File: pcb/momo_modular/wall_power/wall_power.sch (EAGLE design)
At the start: 18 parts

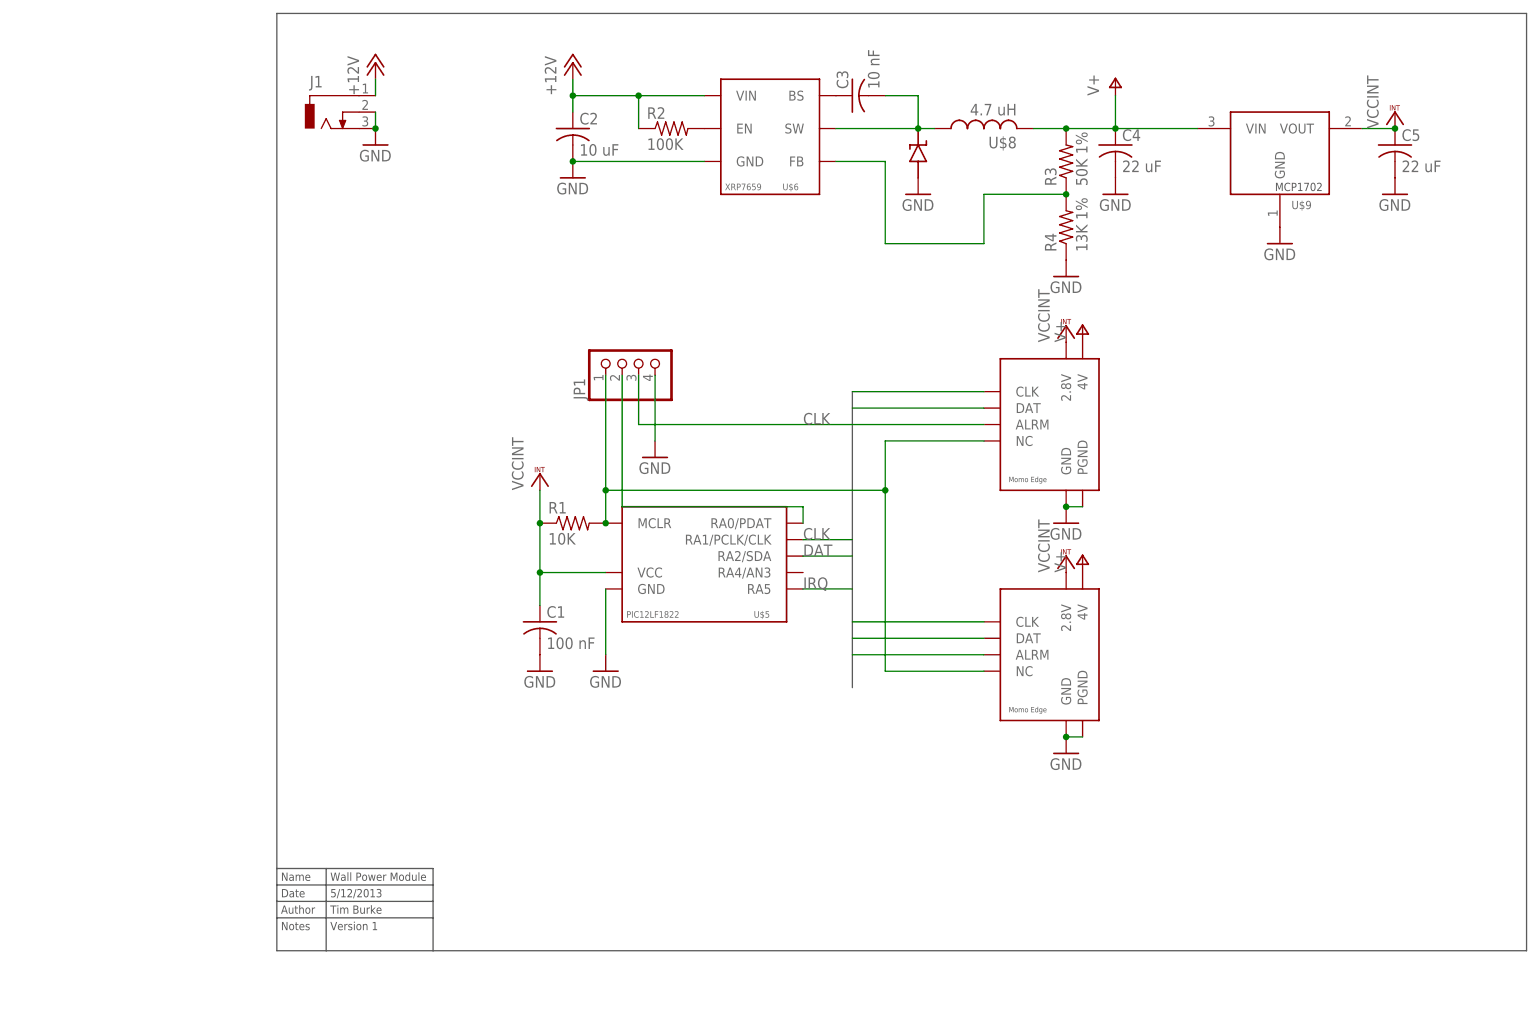
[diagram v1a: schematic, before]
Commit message: Began combining wallpower and controller boards
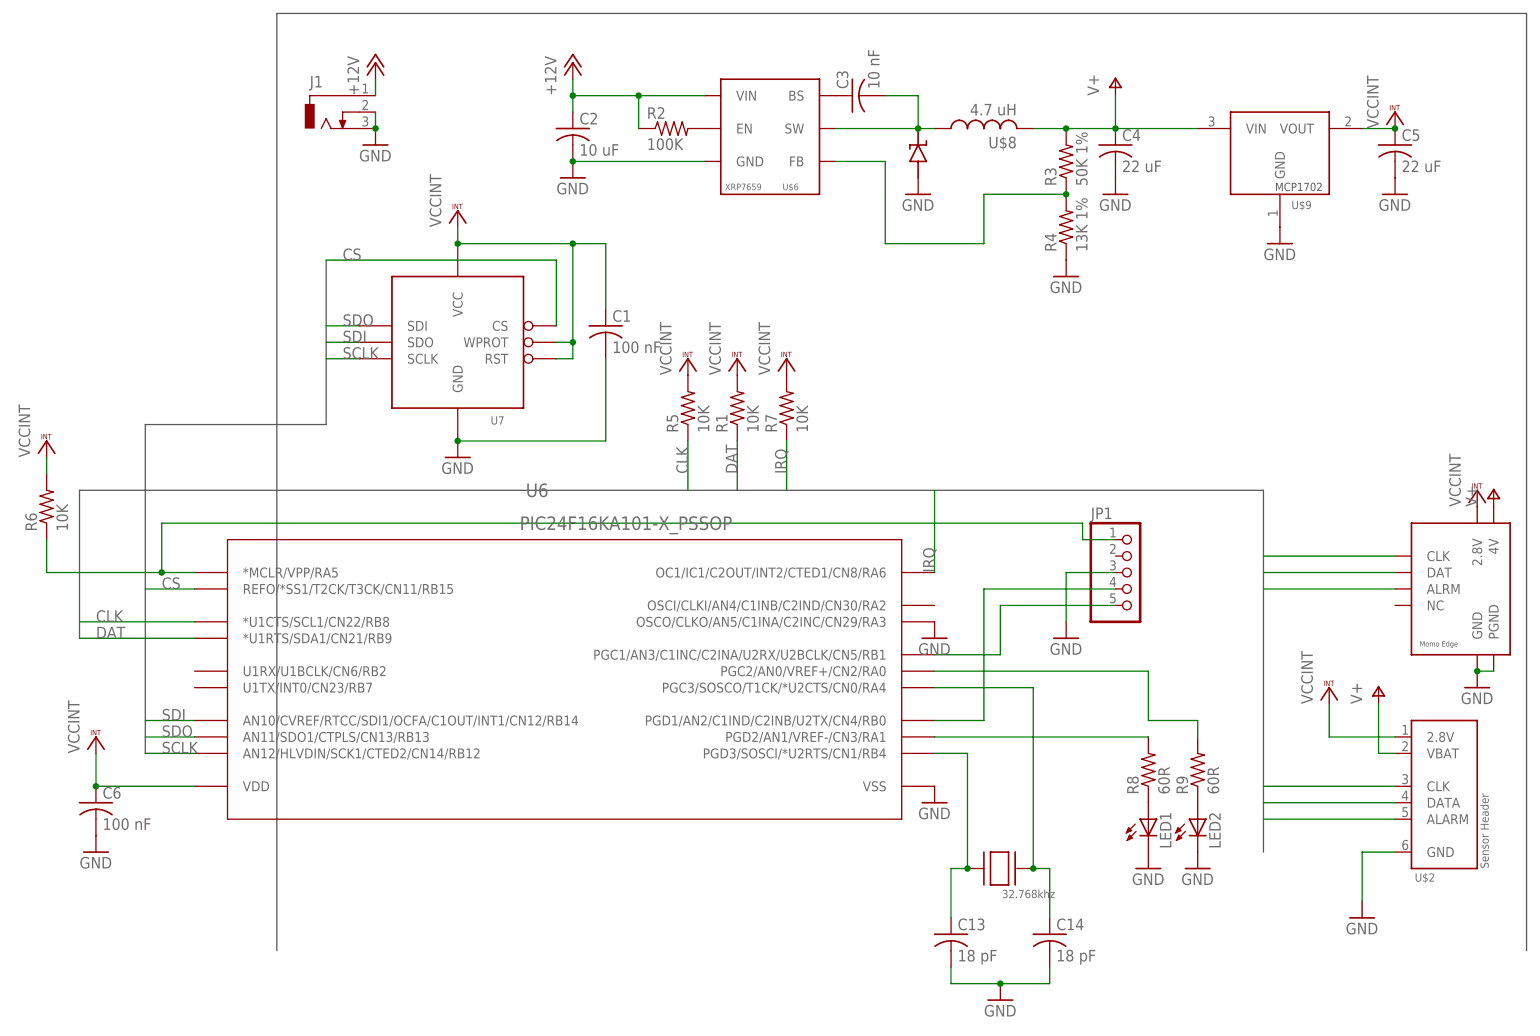
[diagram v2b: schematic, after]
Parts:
- removed U$5: PIC12LF1822, components:PIC12LF1822
- added C13, C14: 18 pF, rcl:C-USC0402K
- added C6: 100 nF, rcl:C-USC0402
- added LED1, LED2: (no value), led:LEDSML0603
- added R5, R6, R7: 10K, rcl:R-US_R0603
- added R8, R9: 60R, rcl:R-US_R0603
- added U6: PIC24F16KA101-X_PSSOP, components:PIC24F16KA101-X_PSSOP
- added U7: FLASH8MSOP8, components:FLASH8MSOP8
- added XTAL1: 32.768khz, components:SMD-XTAL
- JP1: device pinhead:PINHD-1X4 -> pinhead:PINHD-1X5
- U$2: value MOMO-EDGE-8M -> MOMO-SENSOR-HEADER; device components:MOMO-EDGE-8M -> components:MOMO-SENSOR-HEADER
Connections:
- new net CS: U6.REFO/*SS1/T2CK/T3CK/CN11/RB15, U7.CS
- new net N$10: JP1.5, U6.PGC1/AN3/C1INC/C2INA/U2RX/U2BCLK/CN5/RB1
- new net N$15: JP1.1, R6.1, U6.*MCLR/VPP/RA5
- new net N$24: C14.1, U6.PGC3/SOSCO/T1CK/*U2CTS/CN0/RA4, XTAL1.XTAL2
- new net N$25: C13.1, U6.PGD3/SOSCI/*U2RTS/CN1/RB4, XTAL1.XTAL1
- new net N$5: LED2.A, R9.1
- new net N$7: LED1.A, R8.1
- new net N$9: JP1.4, U6.PGD1/AN2/C1IND/C2INB/U2TX/CN4/RB0
- new net SCLK: U6.AN12/HLVDIN/SCK1/CTED2/CN14/RB12, U7.SCLK
- new net SDI: U6.AN10/CVREF/RTCC/SDI1/OCFA/C1OUT/INT1/CN12/RB14, U7.SDO
- new net SDO: U6.AN11/SDO1/CTPLS/CN13/RB13, U7.SDI
- net CLK: now also R5.1, U6.*U1CTS/SCL1/CN22/RB8; no longer JP1.3, U$5.RA1/PCLK/CLK
- net DAT: now also R1.1, U$2.DATA, U6.*U1RTS/SDA1/CN21/RB9; no longer U$2.DAT, U$5.RA2/SDA
- net GND: now also C13.2, C14.2, C6.2, JP1.3, LED1.C, LED2.C, U6.OSCO/CLKO/AN5/C1INA/C2INC/CN29/RA3, U6.VSS, U7.GND; no longer JP1.4, U$2.PGND, U$5.GND
- net IRQ: now also R7.1, U$2.ALARM, U6.OC1/IC1/C2OUT/INT2/CTED1/CN8/RA6; no longer U$2.ALRM, U$5.RA5
- net N$1: now also R9.2, U6.PGC2/AN0/VREF+/CN2/RA0; no longer JP1.1, R1.2, U$1.NC, U$2.NC, U$5.MCLR
- net N$8: now also R8.2, U6.PGD2/AN1/VREF-/CN3/RA1; no longer JP1.2, U$5.RA0/PDAT
- net V+: now also U$2.VBAT; no longer U$2.4V
- net VCCINT: now also C6.1, R1.2, R5.2, R6.2, R7.2, U6.VDD, U7.RST, U7.VCC, U7.WPROT; no longer R1.1, U$5.VCC
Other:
- note removed: "5/12/2013"
- note removed: "Author"
- note removed: "Date"
- note removed: "Name"
- note removed: "Notes"
- note removed: "Tim Burke"
- note removed: "Version 1"
- note removed: "Wall Power Module"
- moved on the sheet: C1, R1

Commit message: Finalized the following boards for fabrication/assembly: Sensor Dev Board GSM Module Combined Wallpower and Controller Boards
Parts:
- removed U$7: DIODE_SS2P3, components:DIODE_SS2P3
- added D1: DIODE_SS2P3SS2P3, components:DIODE_SS2P3SS2P3
- renumbered C13 to C7, C14 to C8, J1 to JP4, U$1 to JP2, U$2 to JP3, U$6 to U1, U$8 to L1, U$9 to U2, U6 to U3, U7 to U4
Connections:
- net GND: now also D1.AN, R8.1, R9.1; no longer LED1.C, LED2.C, U$7.AN
- net N$1: now also LED2.A; no longer R9.2
- net N$2: now also D1.CATH; no longer U$7.CATH
- net N$5: now also LED2.C, R9.2; no longer LED2.A, R9.1
- net N$7: now also LED1.C, R8.2; no longer LED1.A, R8.1
- net N$8: now also LED1.A; no longer R8.2
- net VCCINT: now also JP1.2
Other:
- moved on the sheet: LED1, LED2, R8, R9
